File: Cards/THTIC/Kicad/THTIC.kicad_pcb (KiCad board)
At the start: 2 copper layers, 55.4 x 31.6 mm, 26 parts, among them J1 Conn_01x04_Pin, J2 Plasma 300V, U1 B0509S-1WR3, U2 ISO1540, U3 MCP3221, U4 AMS1117-5, U5 LMV321

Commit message: Final version of THTIC2
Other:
- board text added: "5V SDA SCL GND"
- board text removed: "5V SDA SDL GND"
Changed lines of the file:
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@@
 		)
 	)
-	(gr_text "5V\n\nSDA\n\nSDL\n\nGND"
+	(gr_text "5V\n\nSDA\n\nSCL\n\nGND"
 		(at 194.183 105.156 0)
 		(layer "B.SilkS")

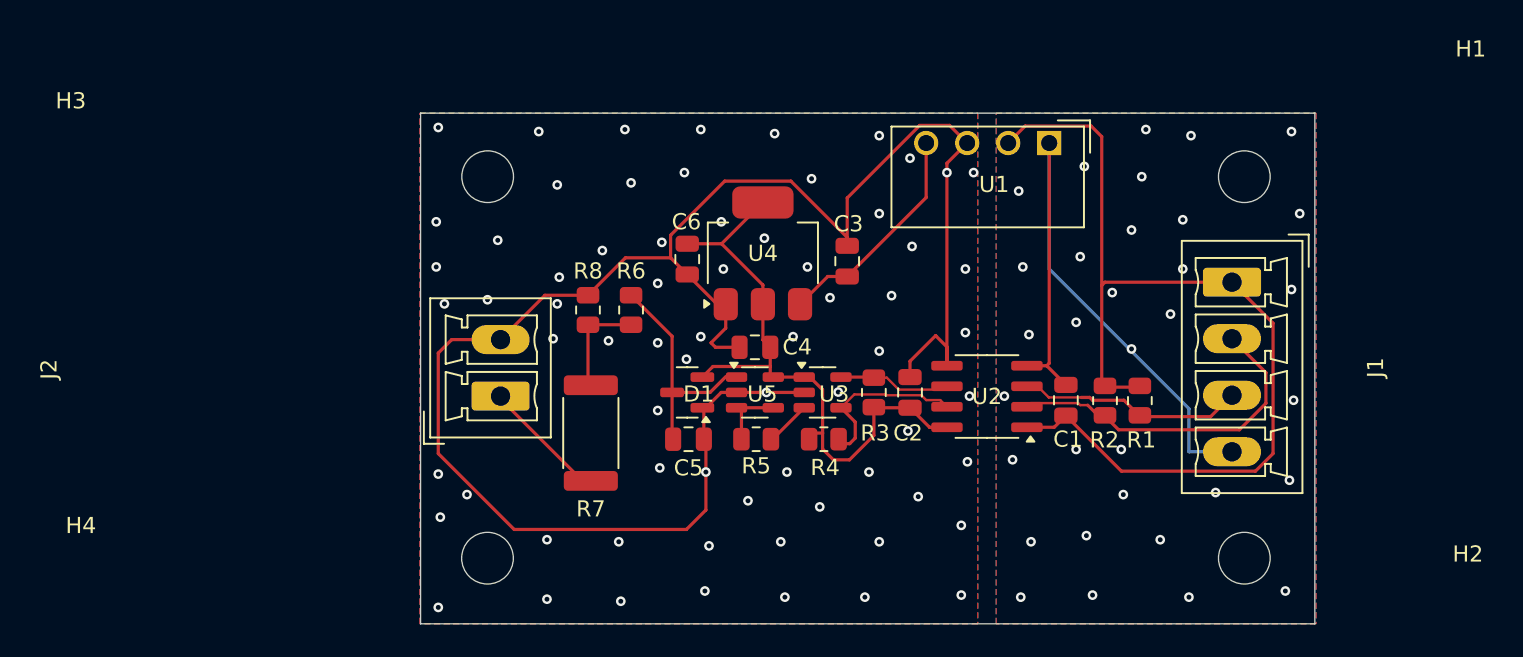
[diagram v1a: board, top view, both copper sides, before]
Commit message: Now measuring 0 - -200 Volts.
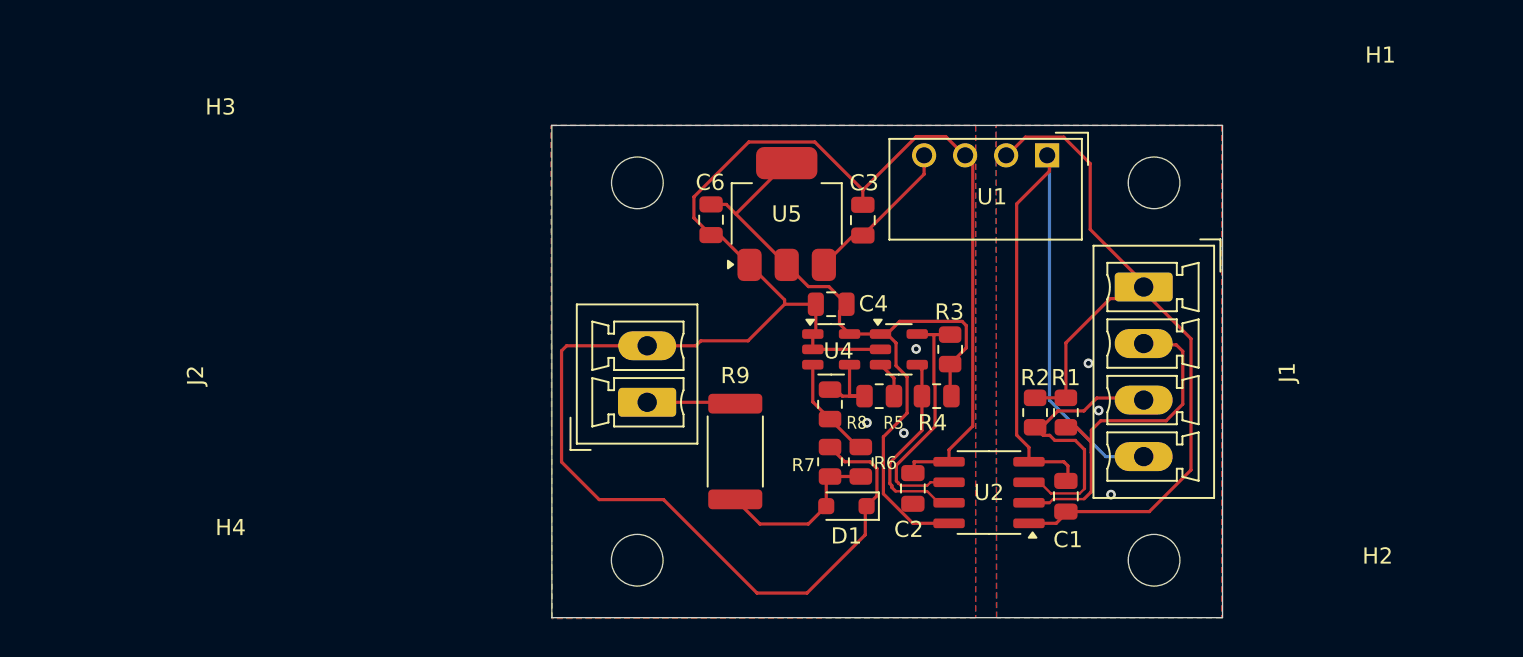
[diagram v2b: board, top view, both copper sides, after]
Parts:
- removed C5: 1nF, Capacitor_SMD:C_0805_2012Metric
- added R8: 100k, Resistor_SMD:R_0805_2012Metric, F.Cu at (172.0, 101.3)
- C6: value 22uF Tant -> 10uF
- D1: value BAT54S -> 5.1V Zener; footprint Package_TO_SOT_SMD:SOT-23 -> Diode_SMD:D_SOD-323_HandSoldering
- J2: value Plasma 300V -> Plasma 200V
- R6: value 10k -> 100k
- moved R7 17.7 mm to (172.0, 104.9)
- moved R6 17.0 mm to (173.9, 104.9)
- moved D1 12.1 mm to (173.0, 107.6)
- moved H3 9.28 mm to (160.0, 87.6)
- moved H4 9.27 mm to (160.0, 111.0)
- moved J2 9.09 mm to (160.6, 101.2)
- moved R9 9.02 mm to (166.1, 104.3), turned to -90 degrees
- moved R5 8.07 mm to (175.0, 100.8)
- moved R4 7.48 mm to (178.6, 100.8), turned to 180 degrees
- moved R2 6.53 mm to (184.7, 101.9)
- moved C2 5.95 mm to (177.1, 106.6)
- moved U2 5.95 mm to (181.8, 106.8)
- moved C1 5.95 mm to (186.6, 107.0)
- moved H1 5.60 mm to (192.0, 87.6)
- moved H2 5.59 mm to (192.0, 111.0)
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- renumbered R2 to R1, R1 to R2, R8 to R7, R7 to R9, U5 to U4, U4 to U5
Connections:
- D1 pad 2: VCC_ISO -> Net-(D1-A)
- R5 pad 2: Net-(U7--) -> Net-(R5-Pad2)
- R6 pad 1: Net-(D2-COM) -> Net-(U4--)
- R6 pad 2: Net-(R10-Pad2) -> Net-(D1-A)
- R7 pad 1: Net-(R10-Pad2) -> Net-(D1-A)
- R9 pad 2: Net-(R10-Pad2) -> Net-(D1-A)
- U4 pad 1: Net-(D2-COM) -> GND_ISO
- U4 pad 3: Net-(U7--) -> Net-(U4--)
- U4 pad 4: Net-(U7--) -> Net-(R5-Pad2)
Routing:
- net Net-(D2-COM): track 14.6 -> 0.00 mm
- net 5V: track 61.5 -> 49.6 mm
- net Net-(D1-A): track 0.00 -> 10.6 mm
- net Net-(U2-SCL2): track 6.63 -> 15.6 mm
- net VCC_ISO: track 38.2 -> 45.5 mm
- net Net-(U4--): track 0.00 -> 6.56 mm
- net Net-(R10-Pad2): track 6.48 -> 0.00 mm
- net Net-(R5-Pad2): track 0.00 -> 5.18 mm
- net Net-(U1-+Vout): track 13.9 -> 9.04 mm
- net Net-(U7--): track 3.96 -> 0.00 mm
- net GND_ISO: track 111.8 -> 115.7 mm, vias 69 -> 3
- net GND: track 42.1 -> 45.9 mm, vias 33 -> 3
- net Net-(J1-Pin_3): track 13.4 -> 16.4 mm
- net Net-(J2-Pin_1): track 7.72 -> 5.49 mm
- net Net-(U2-SDA2): track 10.5 -> 11.8 mm
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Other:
- board size 55.4 x 31.6 mm -> 41.5 x 30.5 mm
- board text added: "+ Varc - Varc"
- board text added: "MetalMusings THTIC March 2025"
- board text removed: "- Varc + Varc"
- board text removed: "MetalMusings THTIC"

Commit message: Gerbers done.
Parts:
- added C5: 100nF, Capacitor_SMD:C_0805_2012Metric, F.Cu at (175.5, 95.1)
- moved U3 0.06 mm to (176.3, 97.9)
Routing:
- net GND_ISO: track 115.7 -> 123.7 mm, vias 3 -> 55
- net VCC_ISO: track 45.5 -> 47.3 mm
- net GND: vias 3 -> 27

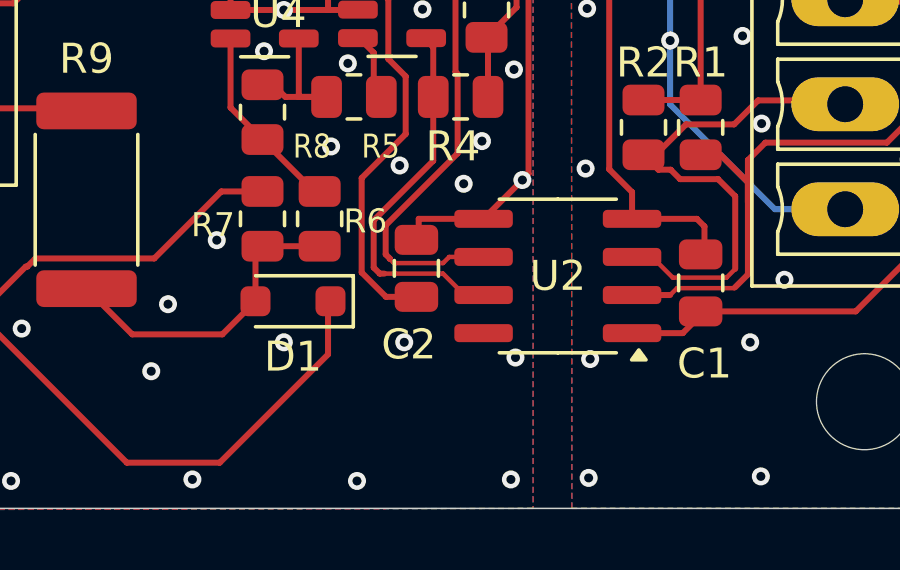
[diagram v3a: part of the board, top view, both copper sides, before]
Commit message: Added missing Viso connection to IS1540
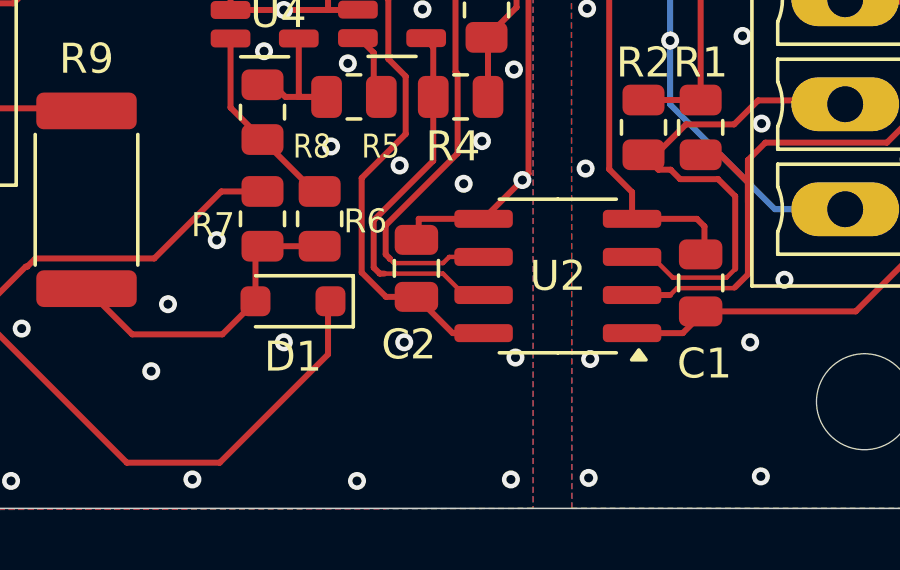
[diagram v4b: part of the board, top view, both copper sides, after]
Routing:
- net VCC_ISO: track 47.3 -> 50.0 mm
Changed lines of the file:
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@@
+	)
+	(segment
+		(start 178.2978 108.712)
+		(end 179.327 108.712)
+		(width 0.2)
+		(layer "F.Cu")
+		(net 5)
 	)
 	(segment
@@
 		(width 0.2)
 		(layer "F.Cu")
+		(net 5)
+	)
+	(segment
+		(start 177.0888 107.503)
+		(end 178.2978 108.712)
+		(width 0.2)
+		(layer "F.Cu")
